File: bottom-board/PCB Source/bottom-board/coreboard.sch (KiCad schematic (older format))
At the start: 22 parts, among them P5 HMI_DATA, P8 SERIAL_DEBUG, U4 AT24CS08-STUM, U9 GR30-SOM

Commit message: rev 0.0.3
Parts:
- removed C72: 100nF, Capacitor_SMD:C_0603_1608Metric, symbol bottom-board-rescue:C_Small
- removed R16: 10K, Resistor_SMD:R_0603_1608Metric, symbol Device:R_Small
- removed U9: GR30-SOM, gr-30:GR30SOM, symbol bottom-board-rescue:GR30-SOM-gr-30
- added C4: 1nF, Capacitor_SMD:C_0603_1608Metric, symbol bottom-board-rescue:C_Small
- added J1: AS0A823-H4SB-7H, Uno:TE_2309407-1, symbol bottom-board-rescue:AS0A823-H4SB-7H
- added R68, R69: 2K7, Resistor_SMD:R_0603_1608Metric, symbol bottom-board-rescue:R_Small
- C31, C59, C60: MPN C1608X7R1E104K080AA -> GCM188R71C104KA37D
- FB12, FB13, FB14, FB15: symbol Device:Ferrite_Bead -> bottom-board-rescue:Ferrite_Bead-Device
- Power1, Reset1, TP1, TP2: symbol Connector:TestPoint -> bottom-board-rescue:TestPoint-Connector
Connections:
- net labels removed: +1V8
- wire segments 137 -> 270
- no-connect marks 92 -> 142
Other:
- note removed: "SoM connections"

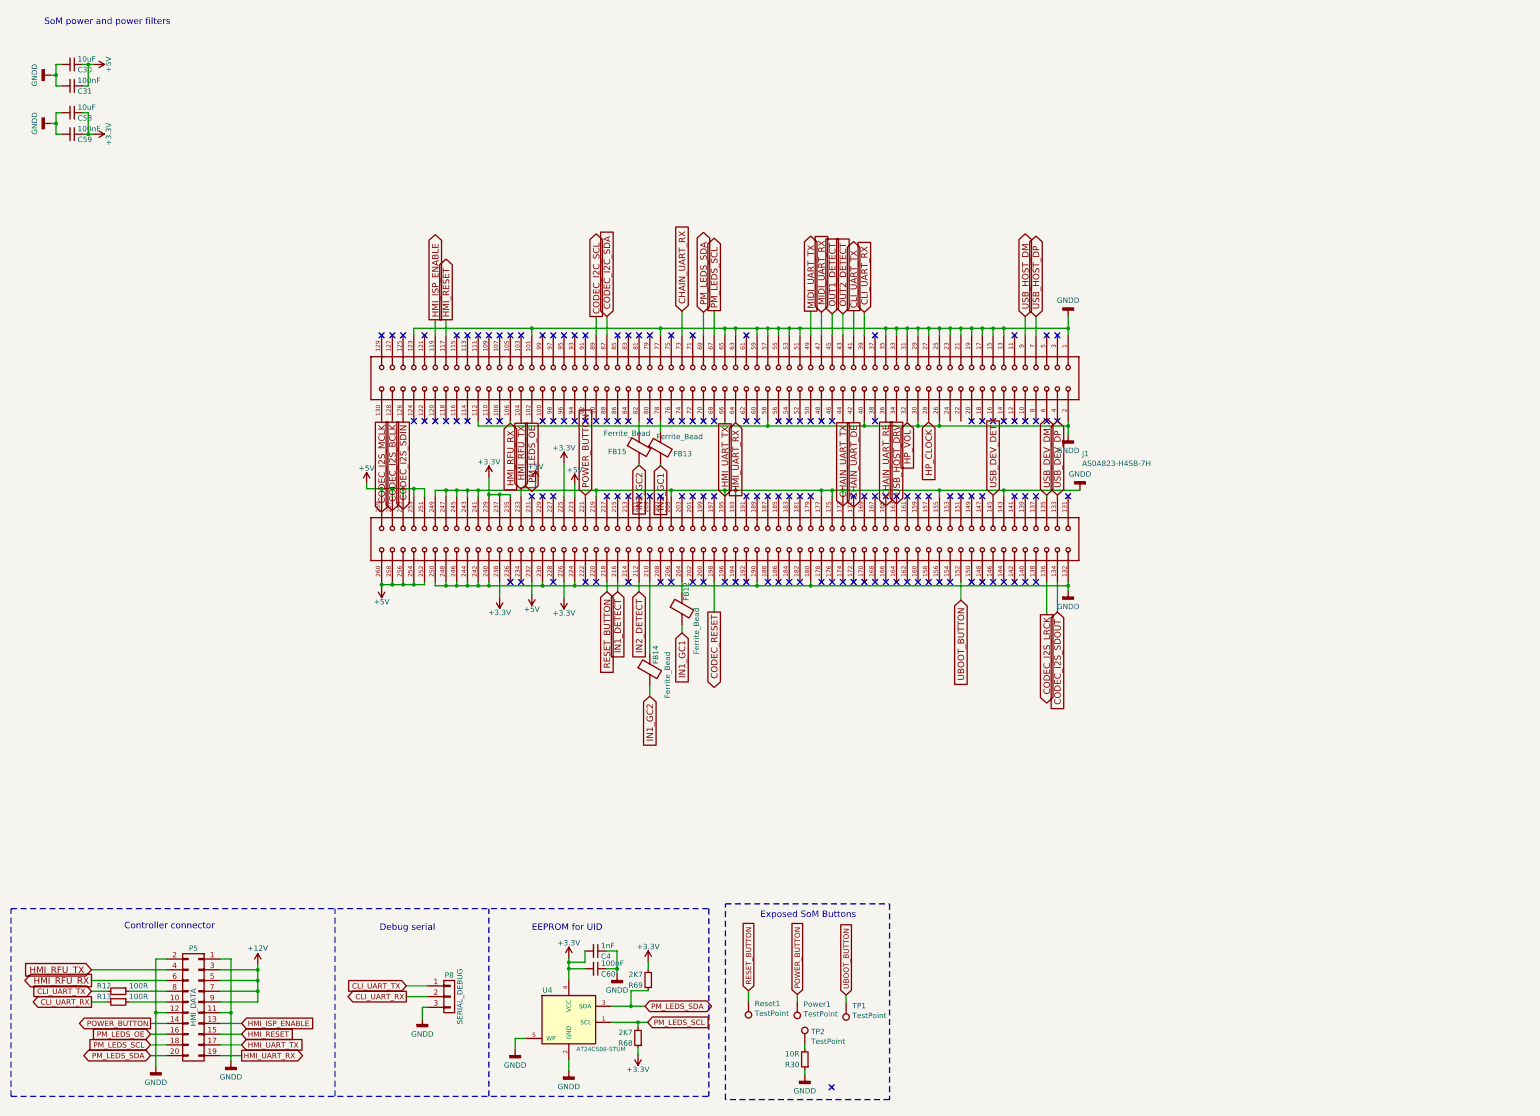
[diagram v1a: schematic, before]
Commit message: change design to 4 layer PCB
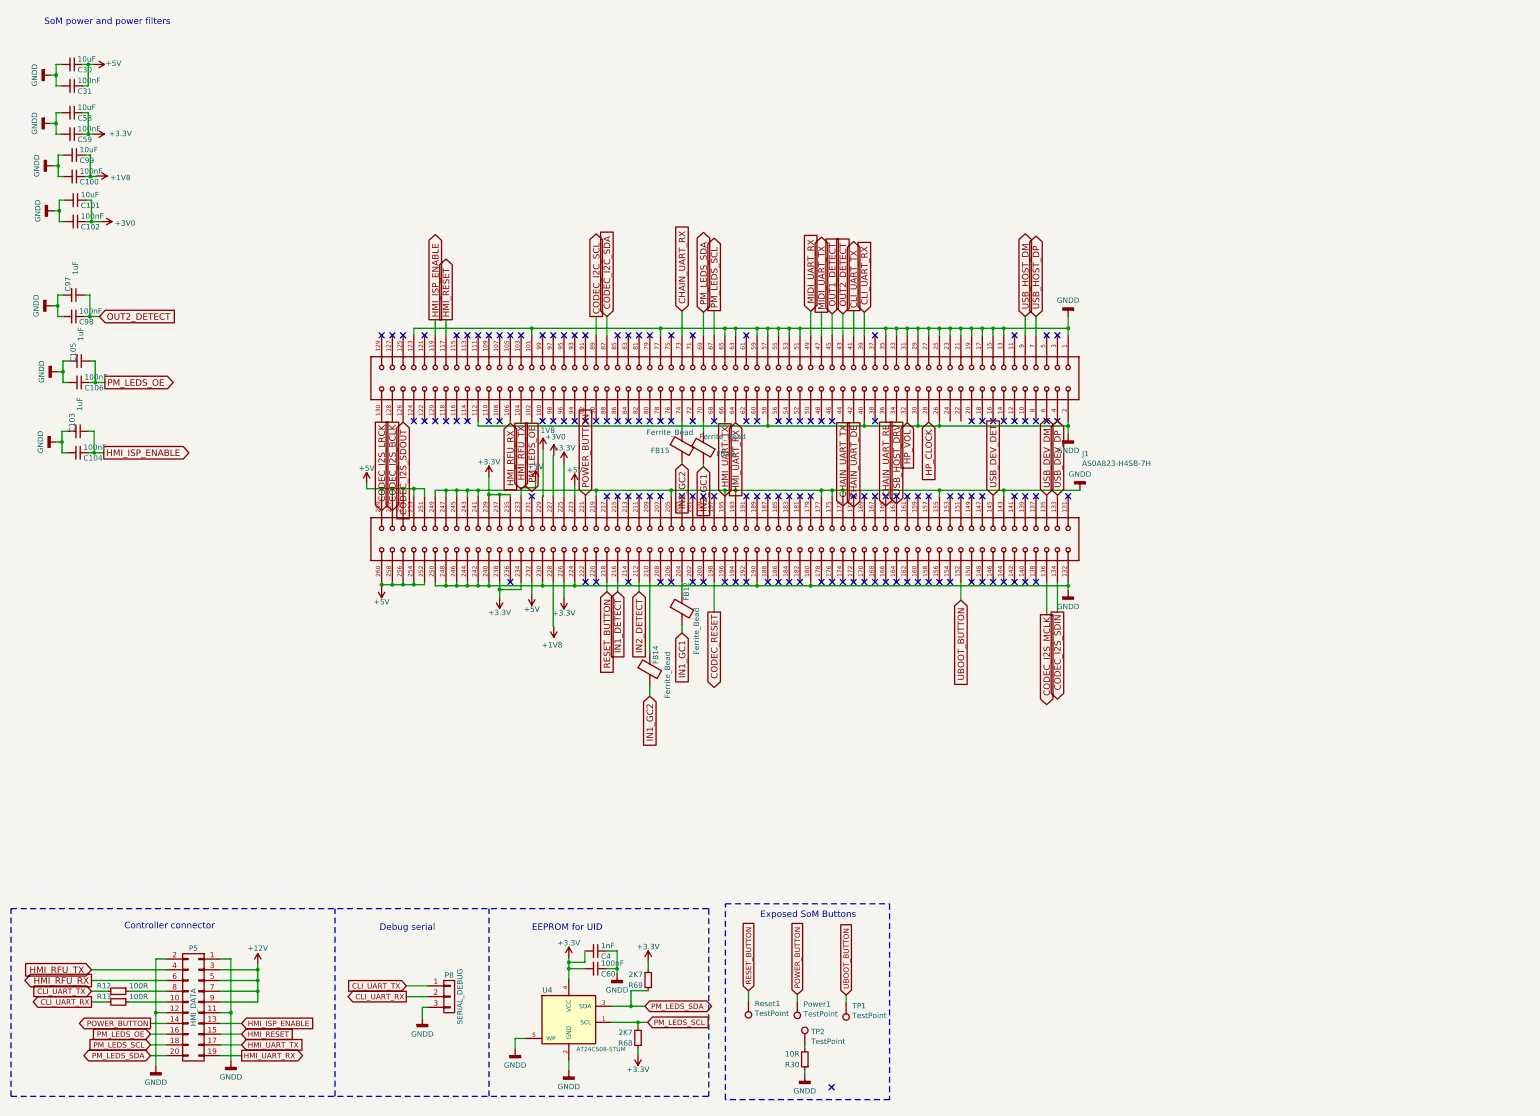
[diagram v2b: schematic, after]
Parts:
- added C100, C102, C104, C106, C98: 100nF, Capacitor_SMD:C_0603_1608Metric, symbol bottom-board-rescue:C_Small
- added C101, C99: 10uF, Capacitor_SMD:C_0805_2012Metric, symbol bottom-board-rescue:C_Small
- added C103, C105, C97: 1uF, Capacitor_SMD:C_0603_1608Metric, symbol bottom-board-rescue:C_Small
- J1: footprint Uno:TE_2309407-1 -> Uno:TE_2309409-1; MPN AS0A823-H4SB-7H -> TE_2309409-1
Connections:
- net +3V3: now also J1.234
- net CODEC_I2S_LRCK: now also J1.130; no longer J1.136
- net CODEC_I2S_MCLK: now also J1.136; no longer J1.130
- net CODEC_I2S_SDIN: now also J1.134; no longer J1.126
- net CODEC_I2S_SDOUT: now also J1.126; no longer J1.134
- net GNDD: now also C100.2, C101.2, C102.2, C103.2, C104.2, C105.2, C106.2, C97.2, C98.2, C99.2
- net HMI_ISP_ENABLE: now also C103.1, C104.1
- net MIDI_UART_RX: now also J1.49; no longer J1.47
- net MIDI_UART_TX: now also J1.47; no longer J1.49
- net OUT2_DETECT: now also C97.1, C98.1
- net PM_LEDS_OE: now also C105.1, C106.1
- net at FB15.1: now also J1.74; no longer J1.82
- net at FB13.1: now also J1.70; no longer J1.78
- net +3V0: now reaches J1.227
- net +3V0: now also C101.1, C102.1
- net +1V8: now reaches J1.228
- net +1V8: now also J1.229, C100.1, C99.1
- no-connect marks 142 -> 138
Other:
- moved on the sheet: FB13, FB15

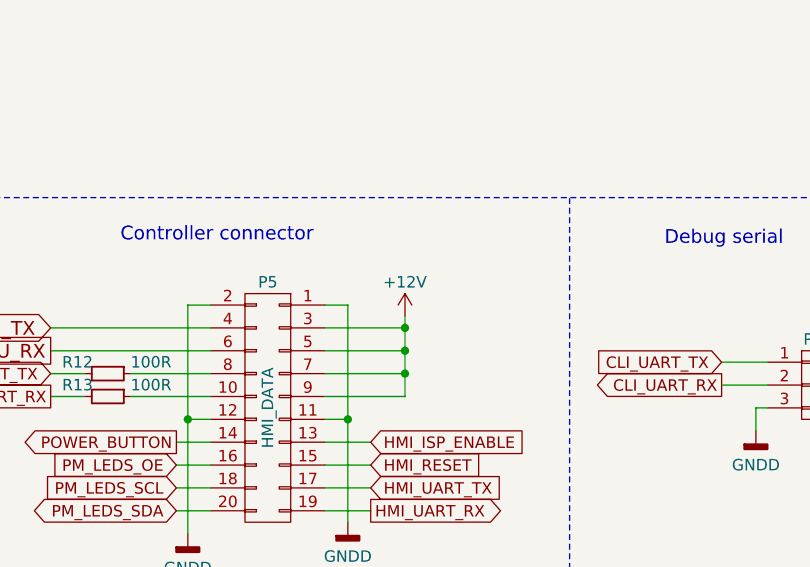
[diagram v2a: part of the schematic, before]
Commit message: supply topboard with 5V instead of 12
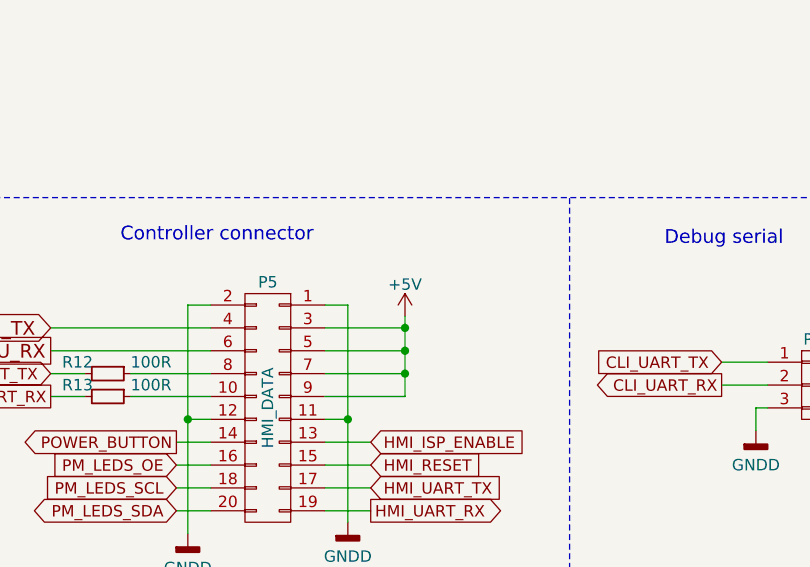
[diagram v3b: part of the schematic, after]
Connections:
- net +12V is gone; now on net +5V: P5.3 (P3), P5.5 (P5), P5.7 (P7), P5.9 (P9)
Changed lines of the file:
@@
 Connection ~ 2100 10005
-$Comp
-L bottom-board-rescue:+12V-power #PWR?
-U 1 1 5F60A18A
-P 3050 9555
-AR Path="/54F72FB8/5F60A18A" Ref="#PWR?"  Part="1"
-AR Path="/54F725AE/5F60A18A" Ref="#PWR0136"  Part="1"
-F 0 "#PWR0136" H 3050 9405 50  0001 C CNN
-F 1 "+12V" H 3050 9705 50  0000 C CNN
-F 2 "" H 3050 9555 60  0000 C CNN
-F 3 "" H 3050 9555 60  0000 C CNN
-	1    3050 9555
-	1    0    0    -1
-$EndComp
 $Comp
 L bottom-board-rescue:R_Small R?
@@
 Text GLabel 1615 4785 2    60   Output ~ 0
 HMI_ISP_ENABLE
+$Comp
+L bottom-board-rescue:+5V-power #PWR?
+U 1 1 5FE59776
+P 3050 9555
+F 0 "#PWR?" H 3050 9405 50  0001 C CNN
+F 1 "+5V" H 3050 9695 50  0000 C CNN
+F 2 "" H 3050 9555 60  0000 C CNN
+F 3 "" H 3050 9555 60  0000 C CNN
+	1    3050 9555
+	1    0    0    -1
+$EndComp
 $EndSCHEMATC

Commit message: cleanup BOM lines
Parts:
- R12, R13: MPN RMCF0603JT100R -> RT0603DRD07100RL
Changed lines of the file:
@@
 Sheet 4 11
 Title "MOD Dwarf - Main Board"
-Date "2019-08-16"
-Rev "0.2"
+Date "2021-04-07"
+Rev "1.2"
 Comp "MOD Devices GmbH"
 Comment1 "Dwarf Audio processing board"
@@
 F 2 "Resistor_SMD:R_0603_1608Metric" H 1750 9805 60  0001 C CNN
 F 3 "" H 1750 9805 60  0000 C CNN
-F 4 "RMCF0603JT100R" H -7000 4455 50  0001 C CNN "MPN"
+F 4 "RT0603DRD07100RL" H -7000 4455 50  0001 C CNN "MPN"
 	1    1750 9805
 	0    1    1    0
@@
 F 2 "Resistor_SMD:R_0603_1608Metric" H 1750 9905 60  0001 C CNN
 F 3 "" H 1750 9905 60  0000 C CNN
-F 4 "RMCF0603JT100R" H -7000 4555 50  0001 C CNN "MPN"
+F 4 "RT0603DRD07100RL" H -7000 4555 50  0001 C CNN "MPN"
 	1    1750 9905
 	0    1    1    0

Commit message: change recovery pads to holes, easier on production
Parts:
- TP1, TP2: footprint TestPoint:TestPoint_Pad_D1.5mm -> TestPoint:TestPoint_Loop_D1.80mm_Drill1.0mm_Beaded
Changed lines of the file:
@@
 F 0 "TP2" H 8208 10418 50  0000 L CNN
 F 1 "TestPoint" H 8208 10327 50  0000 L CNN
-F 2 "TestPoint:TestPoint_Pad_D1.5mm" H 8350 10300 50  0001 C CNN
+F 2 "TestPoint:TestPoint_Loop_D1.80mm_Drill1.0mm_Beaded" H 8350 10300 50  0001 C CNN
 F 3 "~" H 8350 10300 50  0001 C CNN
 	1    8150 10300
@@
 F 0 "TP1" H 8477 9941 50  0000 R CNN
 F 1 "TestPoint" H 8477 10032 50  0000 R CNN
-F 2 "TestPoint:TestPoint_Pad_D1.5mm" H 8735 9915 50  0001 C CNN
+F 2 "TestPoint:TestPoint_Loop_D1.80mm_Drill1.0mm_Beaded" H 8735 9915 50  0001 C CNN
 F 3 "~" H 8735 9915 50  0001 C CNN
 	1    8535 9915

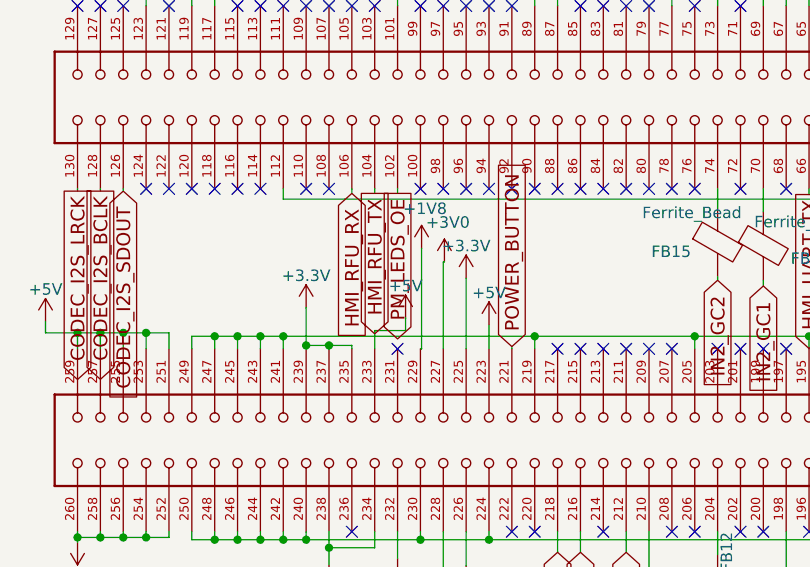
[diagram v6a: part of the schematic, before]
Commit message: give analog bias to PX30 analog reference
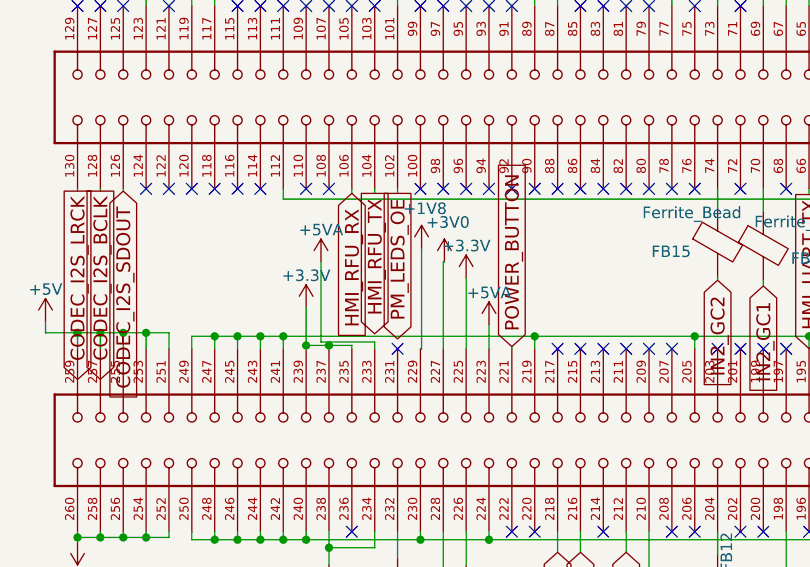
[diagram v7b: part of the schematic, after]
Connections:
- net +5V: no longer J1.223, J1.233
- new net +5VA: J1.223, J1.233
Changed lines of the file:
@@
 Text GLabel 7305 3460 1    60   Output ~ 0
 PM_LEDS_SCL
-Text GLabel 5605 4510 3    60   Output ~ 0
-PM_LEDS_OE
 Text GLabel 2050 10405 0    50   BiDi ~ 0
 PM_LEDS_SDA
@@
 Wire Wire Line
 	6705 6955 6705 7055
-$Comp
-L bottom-board-rescue:AS0A823-H4SB-7H J1
-U 1 1 5F6147C6
-P 7605 4790
-F 0 "J1" V 7609 7920 50  0000 L CNN
-F 1 "AS0A823-H4SB-7H" V 7700 7920 50  0000 L CNN
-F 2 "Uno:TE_2309409-1" H 7605 4790 50  0001 L BNN
-F 3 "None" H 7605 4790 50  0001 L BNN
-F 4 "TE_2309409-1" H 7605 4790 50  0001 L BNN "MPN"
-	1    7605 4790
-	0    1    1    0
-$EndComp
 NoConn ~ 10505 3690
 NoConn ~ 10405 3690
@@
 	6105 5180 6105 5190
 $Comp
-L bottom-board-rescue:+5V-power #PWR0231
-U 1 1 5FEF62CE
-P 6005 5085
-F 0 "#PWR0231" H 6005 4935 50  0001 C CNN
-F 1 "+5V" H 6005 5225 50  0000 C CNN
-F 2 "" H 6005 5085 60  0000 C CNN
-F 3 "" H 6005 5085 60  0000 C CNN
-	1    6005 5085
-	1    0    0    -1
-$EndComp
-$Comp
 L bottom-board-rescue:+5V-power #PWR0232
 U 1 1 5FEFE44D
@@
 $EndComp
 Wire Wire Line
-	5205 5190 5205 5175
-Wire Wire Line
 	5305 5190 5305 5175
 Wire Wire Line
-	5305 5175 5205 5175
-Connection ~ 5205 5175
-Wire Wire Line
-	5205 5175 5205 5010
-Wire Wire Line
 	5405 5190 5405 5175
-Wire Wire Line
-	5405 5175 5305 5175
-Connection ~ 5305 5175
-$Comp
-L bottom-board-rescue:+5V-power #PWR0235
-U 1 1 60058024
-P 5640 5055
-F 0 "#PWR0235" H 5640 4905 50  0001 C CNN
-F 1 "+5V" H 5640 5195 50  0000 C CNN
-F 2 "" H 5640 5055 60  0000 C CNN
-F 3 "" H 5640 5055 60  0000 C CNN
-	1    5640 5055
-	1    0    0    -1
-$EndComp
-Wire Wire Line
-	5505 5190 5505 5110
-Wire Wire Line
-	5505 5110 5640 5110
-Wire Wire Line
-	5640 5110 5640 5055
 NoConn ~ 6305 5190
 NoConn ~ 6405 5190
@@
 Wire Wire Line
 	4505 6015 4405 6015
-$Comp
-L bottom-board-rescue:+5V-power #PWR0246
-U 1 1 603BCCE0
-P 5605 6105
-F 0 "#PWR0246" H 5605 5955 50  0001 C CNN
-F 1 "+5V" H 5605 6245 50  0000 C CNN
-F 2 "" H 5605 6105 60  0000 C CNN
-F 3 "" H 5605 6105 60  0000 C CNN
-	1    5605 6105
-	-1   0    0    1
-$EndComp
-Wire Wire Line
-	5605 5990 5605 6105
 $Comp
 L bottom-board-rescue:+3.3V-power #PWR0247
@@
 	1    0    0    -1
 $EndComp
+Wire Wire Line
+	5205 5175 5205 5010
+Wire Wire Line
+	5205 5190 5205 5175
+Connection ~ 5205 5175
+Wire Wire Line
+	5405 5175 5305 5175
+Wire Wire Line
+	5305 5175 5205 5175
+Connection ~ 5305 5175
+$Comp
+L bottom-board-rescue:AS0A823-H4SB-7H J1
+U 1 1 5F6147C6
+P 7605 4790
+F 0 "J1" V 7609 7920 50  0000 L CNN
+F 1 "AS0A823-H4SB-7H" V 7700 7920 50  0000 L CNN
+F 2 "Uno:TE_2309409-1" H 7605 4790 50  0001 L BNN
+F 3 "None" H 7605 4790 50  0001 L BNN
+F 4 "TE_2309409-1" H 7605 4790 50  0001 L BNN "MPN"
+	1    7605 4790
+	0    1    1    0
+$EndComp
+Text GLabel 5605 4510 3    60   Output ~ 0
+PM_LEDS_OE
+$Comp
+L bottom-board-rescue:+5VA-power #PWR?
+U 1 1 613ED361
+P 5270 4810
+AR Path="/54F7244B/613ED361" Ref="#PWR?"  Part="1"
+AR Path="/54F725AE/613ED361" Ref="#PWR0235"  Part="1"
+F 0 "#PWR0235" H 5270 4660 50  0001 C CNN
+F 1 "+5VA" H 5270 4950 50  0000 C CNN
+F 2 "" H 5270 4810 60  0000 C CNN
+F 3 "" H 5270 4810 60  0000 C CNN
+	1    5270 4810
+	1    0    0    -1
+$EndComp
+Wire Wire Line
+	5505 5190 5505 5160
+Wire Wire Line
+	5505 5160 5270 5160
+Wire Wire Line
+	5270 4810 5270 5160
+$Comp
+L bottom-board-rescue:+5VA-power #PWR?
+U 1 1 614791BA
+P 6005 5085
+AR Path="/54F7244B/614791BA" Ref="#PWR?"  Part="1"
+AR Path="/54F725AE/614791BA" Ref="#PWR0246"  Part="1"
+F 0 "#PWR0246" H 6005 4935 50  0001 C CNN
+F 1 "+5VA" H 6005 5225 50  0000 C CNN
+F 2 "" H 6005 5085 60  0000 C CNN
+F 3 "" H 6005 5085 60  0000 C CNN
+	1    6005 5085
+	1    0    0    -1
+$EndComp
+Wire Wire Line
+	5605 5990 5605 6105
+$Comp
+L bottom-board-rescue:+5V-power #PWR0231
+U 1 1 614A179C
+P 5605 6105
+F 0 "#PWR0231" H 5605 5955 50  0001 C CNN
+F 1 "+5V" H 5605 6245 50  0000 C CNN
+F 2 "" H 5605 6105 60  0000 C CNN
+F 3 "" H 5605 6105 60  0000 C CNN
+	1    5605 6105
+	-1   0    0    1
+$EndComp
 $EndSCHEMATC
